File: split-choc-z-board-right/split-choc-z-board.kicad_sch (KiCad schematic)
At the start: 79 parts, among them J1 USB4105-GF-A, J2 USB4105-GF-A, SW1 SW_SPST, SW10 SW_SPST, SW11 SW_SPST, SW12 SW_SPST, SW13 SW_SPST, SW14 SW_SPST, SW15 SW_SPST, SW16 SW_SPST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

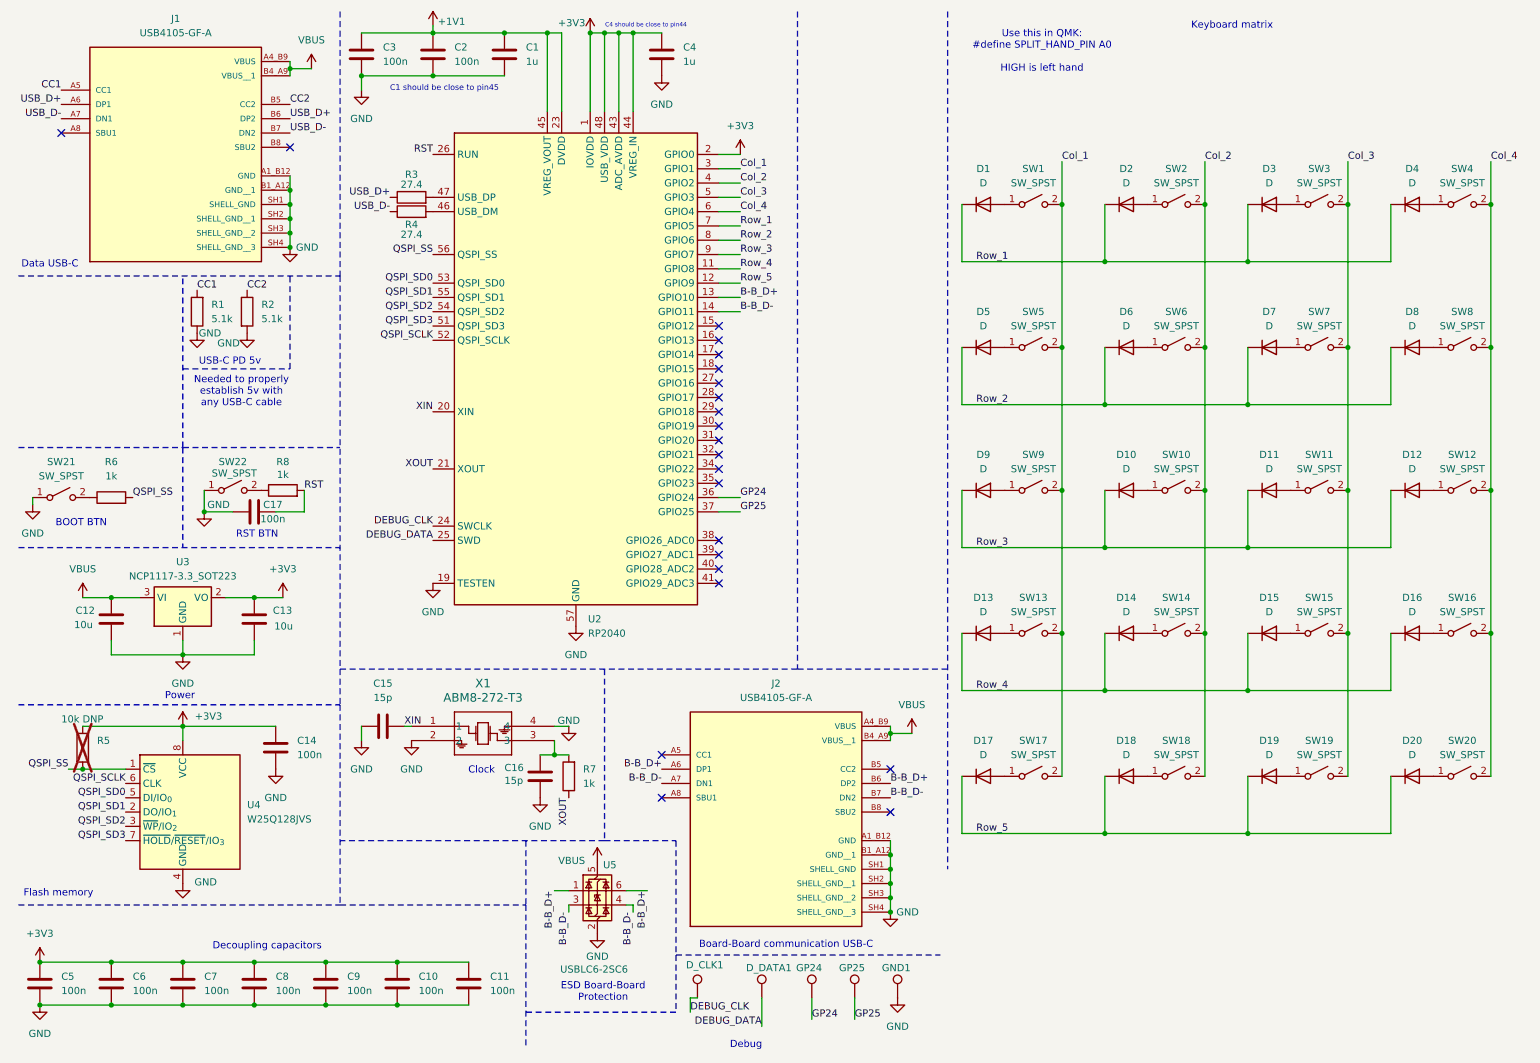
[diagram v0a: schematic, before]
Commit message: Updated right side schematic to match left
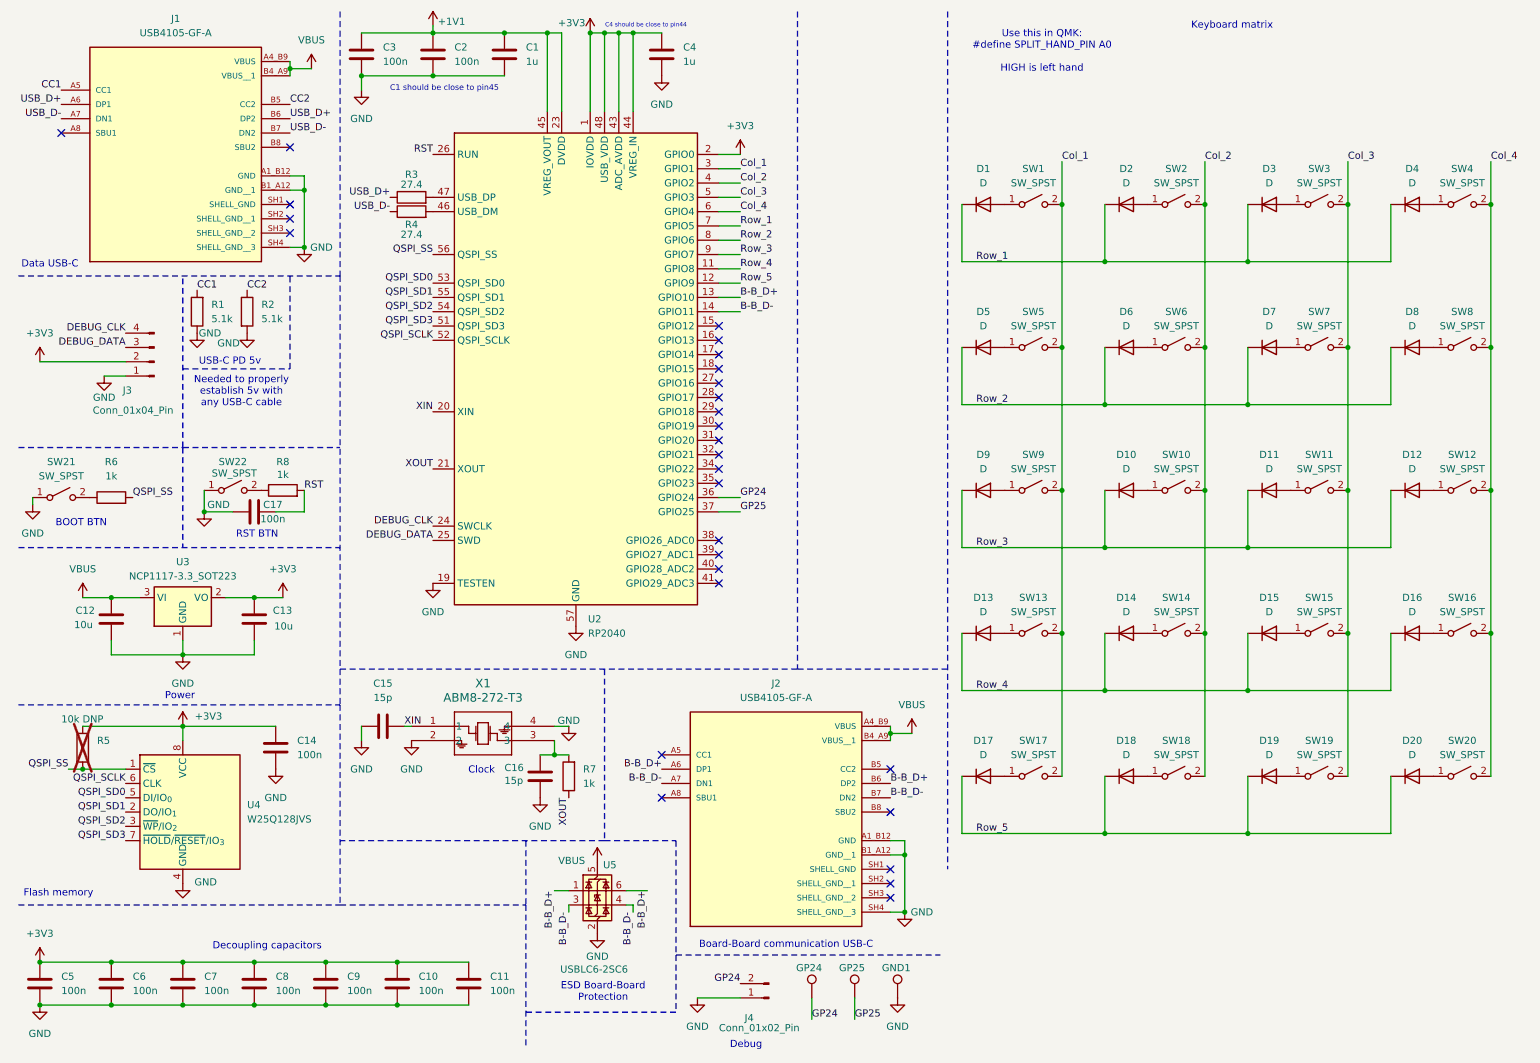
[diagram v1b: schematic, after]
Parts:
- removed D_CLK1, D_DATA1: TestPoint, TestPoint:TestPoint_Pad_D2.0mm, symbol Connector:TestPoint
- added J3: Conn_01x04_Pin, Connector_PinHeader_2.54mm:PinHeader_1x04_P2.54mm_Vertical, symbol Connector:Conn_01x04_Pin
- added J4: Conn_01x02_Pin, Connector_PinHeader_2.54mm:PinHeader_1x02_P2.54mm_Vertical, symbol Connector:Conn_01x02_Pin
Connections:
- net +3V3: now also J3.2 (Pin_2)
- net DEBUG_CLK: now also J3.4 (Pin_4)
- net DEBUG_DATA: now also J3.3 (Pin_3)
- net GND: now also J3.1 (Pin_1), J4.1 (Pin_1); no longer J1.SH1 (SHELL_GND), J1.SH2 (SHELL_GND__1), J1.SH3 (SHELL_GND__2), J2.SH1 (SHELL_GND), J2.SH2 (SHELL_GND__1), J2.SH3 (SHELL_GND__2)
- net GP24: now also J4.2 (Pin_2)
- no-connect marks 22 -> 28
